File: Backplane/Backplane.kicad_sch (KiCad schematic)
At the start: 16 parts

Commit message: Backplane: Fix couple of errors
Fix messed up AR lines, add jumper to activate /AR15. Layout WIP (no power yet)
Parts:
- added JP1: Experimental, Connector_PinHeader_2.54mm:PinHeader_1x02_P2.54mm_Vertical, symbol Jumper:Jumper_2_Open
- added unit 2 of U_A5
- added unit 1 of U_B1
- added unit 2 of U_B5
- added unit 3 of U_B5
- J2: renamed from J?; footprint (none) -> Connector_IDC:IDC-Header_2x25_P2.54mm_Vertical
- R1, R2, R3, R4: renamed from R?; footprint (none) -> Resistor_THT:R_Axial_DIN0207_L6.3mm_D2.5mm_P10.16mm_Horizontal
- U_A1: footprint Package_DIP:DIP-28_W15.24mm -> Package_DIP:DIP-24_W10.16mm
- U_A2: footprint (none) -> DIP-16_W7.62mm
- U_A3, U_A4, U_A5, U_B1, U_B2, U_B3, U_B4, U_B5: footprint (none) -> Package_DIP:DIP-14_W7.62mm
- gave numbers to parts that had none: 1
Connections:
- net Gnd is gone; now on net GND: U_A2.7 (Gnd), U_A2.7 (Gnd)
- net Vcc is gone; now on net +5V: U_A2.14 (Vcc), U_A2.14 (Vcc)
- net GND: now also U_A5.10, U_A5.12, U_A5.13, U_A5.9, U_B1.1, U_B5.10, U_B5.4, U_B5.5, U_B5.9
- net Sys.~{RA_{11}}: no longer U_B2.13
- net Sys.~{RA_{13}}: now also J2.20 (Pin_20)
- net Sys.~{RA_{14}}: now also U_B2.13
- net Sys.~{RA_{15}}: now also JP1.2 (B)
- net at R1.2, R2.1, U_B3.5: now also JP1.1 (A)
- no-connect marks 13 -> 16
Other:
- moved on the sheet: R1, R2

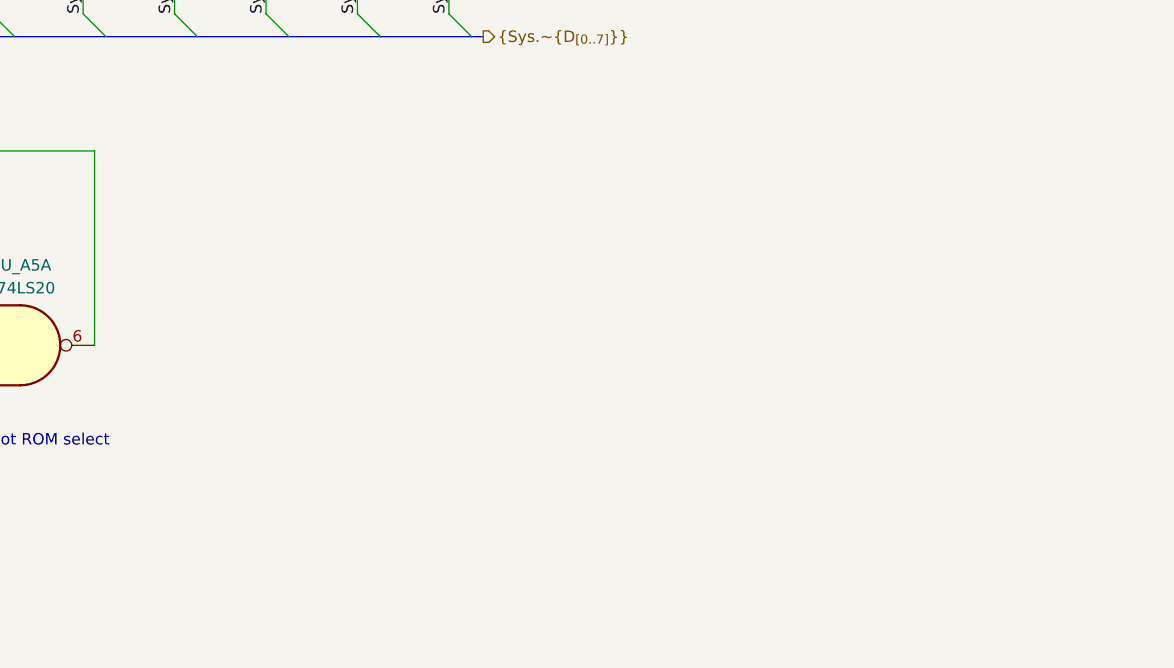
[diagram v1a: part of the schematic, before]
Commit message: Backplane: Completed
Full board layout
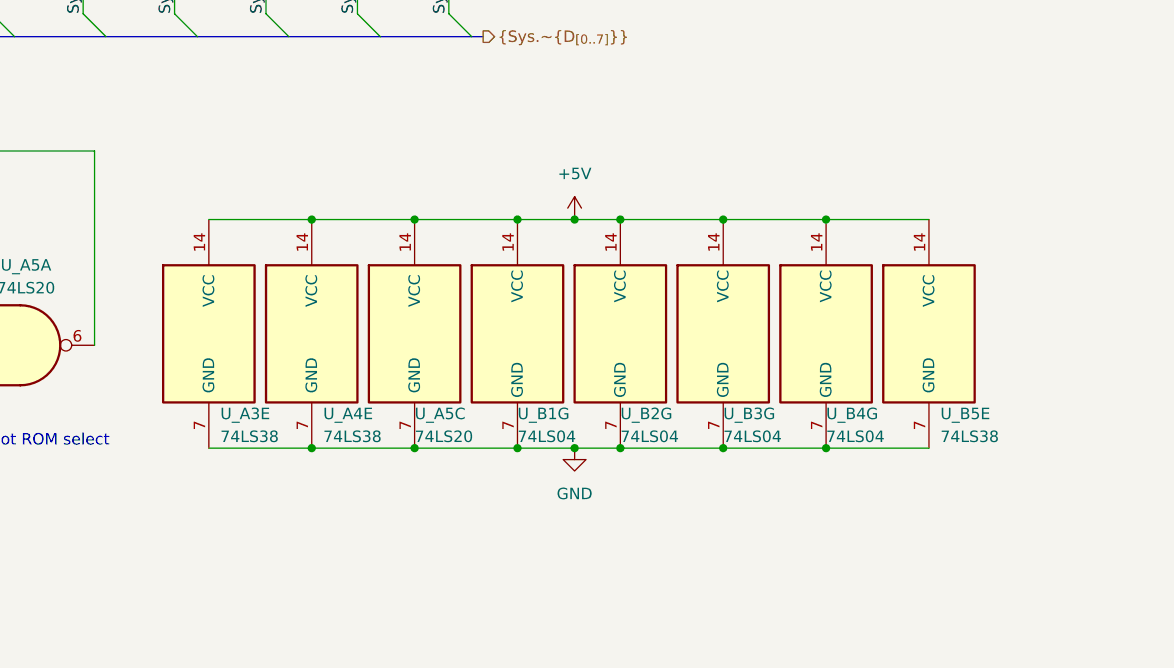
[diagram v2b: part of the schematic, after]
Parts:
- added unit 5 of U_A3
- added unit 5 of U_A4
- added unit 3 of U_A5
- added unit 7 of U_B1
- added unit 7 of U_B2
- added unit 7 of U_B3
- added unit 7 of U_B4
- added unit 5 of U_B5
- U_A2: footprint DIP-16_W7.62mm -> Package_DIP:DIP-14_W7.62mm
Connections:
- net +5V: now also U_A3.14 (VCC), U_A4.14 (VCC), U_A5.14 (VCC), U_B1.14 (VCC), U_B2.14 (VCC), U_B3.14 (VCC), U_B4.14 (VCC), U_B5.14 (VCC)
- net GND: now also U_A3.7 (GND), U_A4.7 (GND), U_A5.7 (GND), U_B1.7 (GND), U_B2.7 (GND), U_B3.7 (GND), U_B4.7 (GND), U_B5.7 (GND)

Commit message: Backplane: Polish up
Annotate connectors on silk screen, change ROM footprint to socketed one
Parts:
- U_A1: footprint Package_DIP:DIP-24_W10.16mm -> Package_DIP:DIP-24_W10.16mm_Socket
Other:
- title: (none) -> Centurion backplane, short
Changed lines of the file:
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@@
 (kicad_sch (version 20211123) (generator eeschema)
   (paper "A4")
+  (title_block
+    (title "Centurion backplane, short")
+    (rev "1.0")
+  )
   (junction (at 19.05 107.95) (diameter 0) (color 0 0 0 0)
   )
@@
   (symbol (lib_id "power:+5V") (at 236.22 125.73 0) (unit 1)
     (in_bom yes) (on_board yes) (fields_autoplaced)
-    (property "Reference" "#PWR?" (id 0) (at 236.22 129.54 0)
+    (property "Reference" "#PWR0123" (id 0) (at 236.22 129.54 0)
       (effects (font (size 1.27 1.27)) hide)
     )
@@
       (effects (font (size 1.27 1.27)) (justify left))
     )
-    (property "Footprint" "Package_DIP:DIP-24_W10.16mm" (id 2) (at 210.82 74.93 0)
+    (property "Footprint" "Package_DIP:DIP-24_W10.16mm_Socket" (id 2) (at 210.82 74.93 0)
       (effects (font (size 1.27 1.27)) hide)
     )
@@
       (reference "#PWR0122") (unit 1) (value "GND") (footprint "")
     )
+    (path "/bd3178ab-c3d1-48e2-8657-6f2f9c3f17fc"
+      (reference "#PWR0123") (unit 1) (value "+5V") (footprint "")
+    )
     (path "/92741a45-2c80-49a0-b822-dc307fb28e0e"
       (reference "#PWR0124") (unit 1) (value "GND") (footprint "")
     )
-    (path "/bd3178ab-c3d1-48e2-8657-6f2f9c3f17fc"
-      (reference "#PWR?") (unit 1) (value "+5V") (footprint "")
-    )
     (path "/2fae2e1f-a694-4160-a6f3-1a6beed67fe7"
       (reference "J1") (unit 1) (value "Front panel") (footprint "Connector_IDC:IDC-Header_2x25_P2.54mm_Vertical")
@@
     )
     (path "/d8a6c379-193f-4aef-93b8-a8eb5ed3d15a"
-      (reference "U_A1") (unit 1) (value "3604") (footprint "Package_DIP:DIP-24_W10.16mm")
+      (reference "U_A1") (unit 1) (value "3604") (footprint "Package_DIP:DIP-24_W10.16mm_Socket")
     )
     (path "/c4c90f89-c7ff-49fa-b875-d46a735819c8"

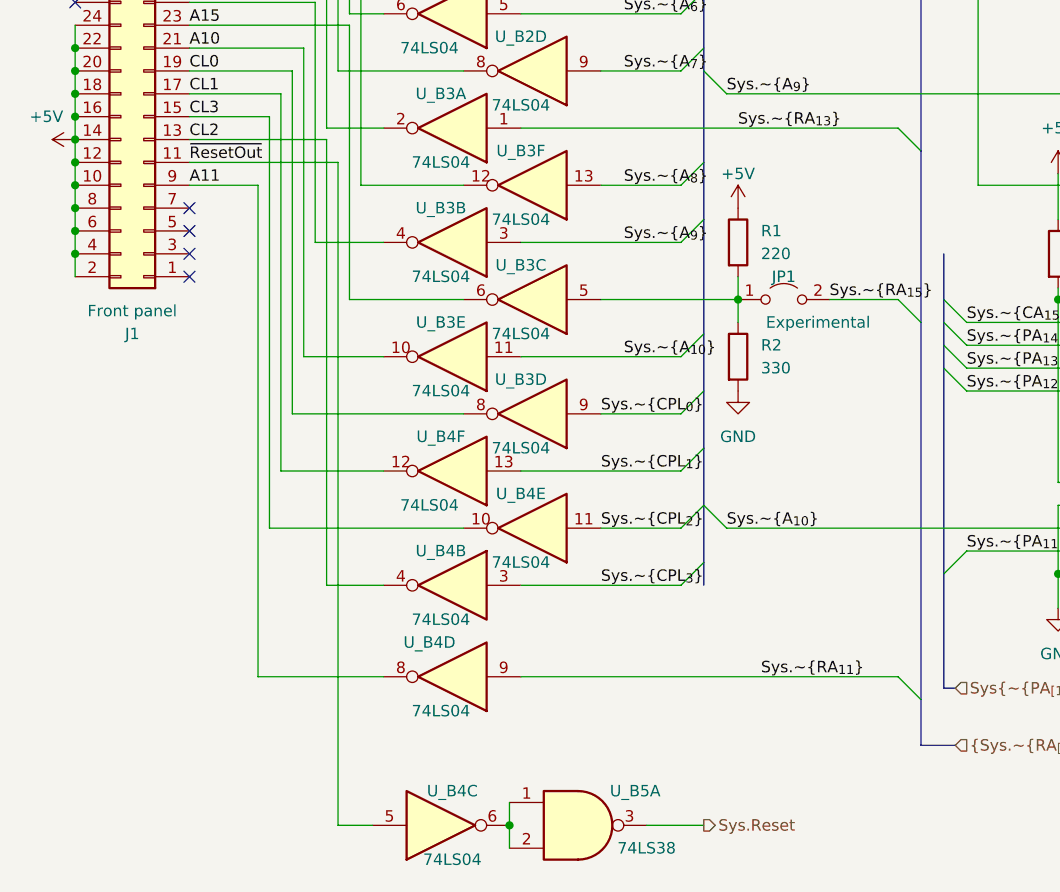
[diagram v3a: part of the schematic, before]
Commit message: Backplane: Fix RA15 signal
Original schematic by Nakazoto contained an error, which has been fixed. So no
need for an experimental jumper on RA15 line; and 220-330 divider actually sits
on a Reset signal, coming from the front panel.
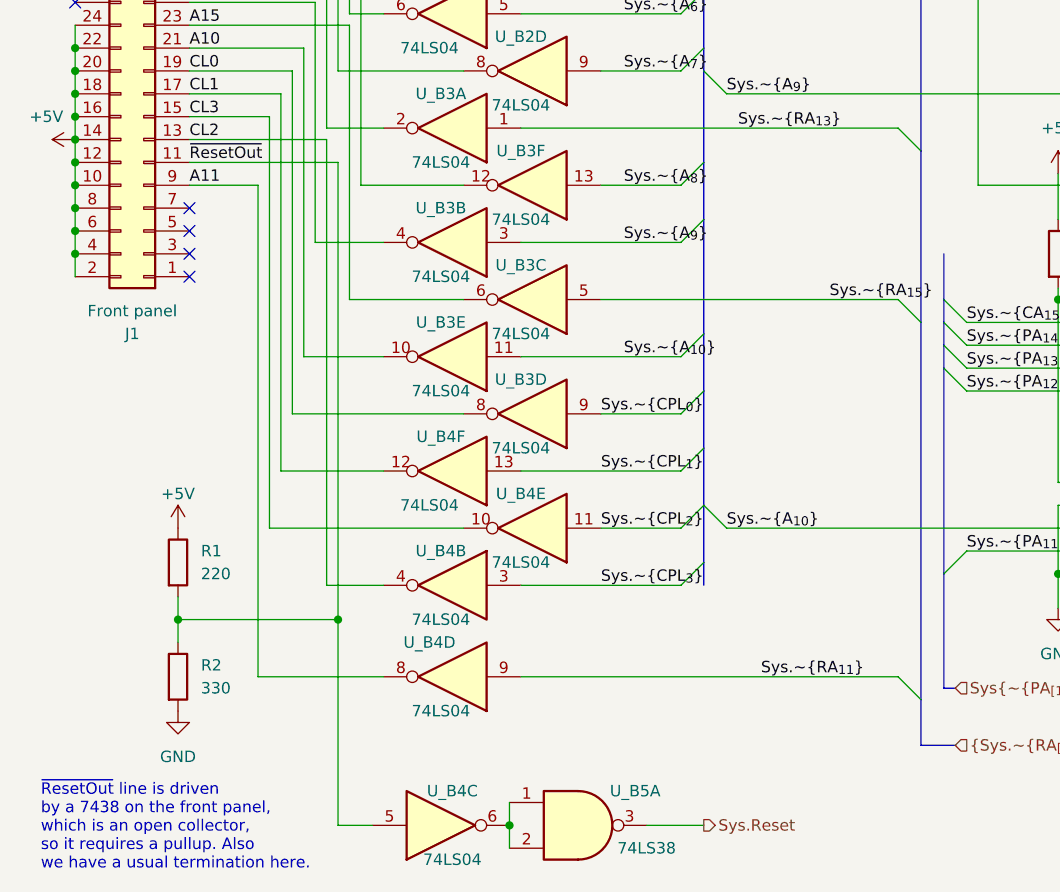
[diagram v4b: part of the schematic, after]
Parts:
- removed JP1: Experimental, Connector_PinHeader_2.54mm:PinHeader_1x02_P2.54mm_Vertical, symbol Jumper:Jumper_2_Open
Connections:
- net Sys.~{RA_{15}}: now also U_B3.5
- net ~{ResetOut}: now also R1.2, R2.1
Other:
- note added: "~{ResetOut} line is driven by a 7438 on the front panel, which is an open collector, so it requires a pullup. Also we have a usual termination here."

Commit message: Backplane: Modular design
Make sure that a horizontal bus connector can be installed, thus extending this
shortened backplane PCB to a full size, if PCB-mounted edge slots can be
purchased.
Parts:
- J2: footprint Connector_IDC:IDC-Header_2x25_P2.54mm_Vertical -> Connector_PinHeader_2.54mm:PinHeader_2x25_P2.54mm_Horizontal
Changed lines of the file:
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@@
     (property "Reference" "J2" (id 0) (at 256.54 21.59 0))
     (property "Value" "System bus" (id 1) (at 256.54 24.13 0))
-    (property "Footprint" "Connector_IDC:IDC-Header_2x25_P2.54mm_Vertical" (id 2) (at 255.27 58.42 0)
+    (property "Footprint" "Connector_PinHeader_2.54mm:PinHeader_2x25_P2.54mm_Horizontal" (id 2) (at 255.27 58.42 0)
       (effects (font (size 1.27 1.27)) hide)
     )
@@
     )
     (path "/3c650ba4-b8b7-493f-9028-99f0e30e52ce"
-      (reference "J2") (unit 1) (value "System bus") (footprint "Connector_IDC:IDC-Header_2x25_P2.54mm_Vertical")
+      (reference "J2") (unit 1) (value "System bus") (footprint "Connector_PinHeader_2.54mm:PinHeader_2x25_P2.54mm_Horizontal")
     )
     (path "/2da09754-df0a-400a-aca6-b8f5a82d0ae3"

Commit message: Backplane: Erratum E001
Incorrect U_A1 chip width
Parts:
- U_A1: footprint Package_DIP:DIP-24_W10.16mm_Socket -> Package_DIP:DIP-24_W15.24mm
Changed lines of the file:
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@@
   (title_block
     (title "Centurion backplane, short")
-    (rev "1.0")
+    (rev "2.0")
   )
   (junction (at 19.05 107.95) (diameter 0) (color 0 0 0 0)
@@
       (effects (font (size 1.27 1.27)) (justify left))
     )
-    (property "Footprint" "Package_DIP:DIP-24_W10.16mm_Socket" (id 2) (at 210.82 74.93 0)
+    (property "Footprint" "Package_DIP:DIP-24_W15.24mm" (id 2) (at 210.82 74.93 0)
       (effects (font (size 1.27 1.27)) hide)
     )
@@
     )
     (path "/d8a6c379-193f-4aef-93b8-a8eb5ed3d15a"
-      (reference "U_A1") (unit 1) (value "3604") (footprint "Package_DIP:DIP-24_W10.16mm_Socket")
+      (reference "U_A1") (unit 1) (value "3604") (footprint "Package_DIP:DIP-24_W15.24mm")
     )
     (path "/c4c90f89-c7ff-49fa-b875-d46a735819c8"

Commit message: Backplane: Use socket for U_A1
Just for compliance, let's change U_A1 footprint to socket
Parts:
- U_A1: footprint Package_DIP:DIP-24_W15.24mm -> Package_DIP:DIP-24_W15.24mm_Socket
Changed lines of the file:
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@@
       (effects (font (size 1.27 1.27)) (justify left))
     )
-    (property "Footprint" "Package_DIP:DIP-24_W15.24mm" (id 2) (at 210.82 74.93 0)
+    (property "Footprint" "Package_DIP:DIP-24_W15.24mm_Socket" (id 2) (at 210.82 74.93 0)
       (effects (font (size 1.27 1.27)) hide)
     )
@@
     )
     (path "/d8a6c379-193f-4aef-93b8-a8eb5ed3d15a"
-      (reference "U_A1") (unit 1) (value "3604") (footprint "Package_DIP:DIP-24_W15.24mm")
+      (reference "U_A1") (unit 1) (value "3604") (footprint "Package_DIP:DIP-24_W15.24mm_Socket")
     )
     (path "/c4c90f89-c7ff-49fa-b875-d46a735819c8"

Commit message: Backplane: Update footprint in the schematic
Update footprint association, synchronize with the PCB. Add one more replacement
entry to the README
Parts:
- U_A3, U_A4, U_A5, U_B1, U_B2, U_B3, U_B4, U_B5: footprint (none) -> Package_DIP:DIP-14_W7.62mm
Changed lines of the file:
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@@
       (effects (font (size 1.27 1.27)) (justify left))
     )
-    (property "Footprint" "" (id 2) (at 218.44 138.43 0)
+    (property "Footprint" "Package_DIP:DIP-14_W7.62mm" (id 2) (at 218.44 138.43 0)
       (effects (font (size 1.27 1.27)) hide)
     )
@@
       (effects (font (size 1.27 1.27)) (justify left))
     )
-    (property "Footprint" "" (id 2) (at 264.16 138.43 0)
+    (property "Footprint" "Package_DIP:DIP-14_W7.62mm" (id 2) (at 264.16 138.43 0)
       (effects (font (size 1.27 1.27)) hide)
     )
@@
       (effects (font (size 1.27 1.27)) (justify left))
     )
-    (property "Footprint" "" (id 2) (at 275.59 138.43 0)
+    (property "Footprint" "Package_DIP:DIP-14_W7.62mm" (id 2) (at 275.59 138.43 0)
       (effects (font (size 1.27 1.27)) hide)
     )
@@
     (property "Reference" "U_B5" (id 0) (at 35.56 36.83 0))
     (property "Value" "74LS38" (id 1) (at 35.56 39.37 0))
-    (property "Footprint" "" (id 2) (at 27.94 41.91 0)
+    (property "Footprint" "Package_DIP:DIP-14_W7.62mm" (id 2) (at 27.94 41.91 0)
       (effects (font (size 1.27 1.27)) hide)
     )
@@
       (effects (font (size 1.27 1.27)) (justify left))
     )
-    (property "Footprint" "" (id 2) (at 229.87 138.43 0)
+    (property "Footprint" "Package_DIP:DIP-14_W7.62mm" (id 2) (at 229.87 138.43 0)
       (effects (font (size 1.27 1.27)) hide)
     )
@@
       (effects (font (size 1.27 1.27)) (justify left))
     )
-    (property "Footprint" "" (id 2) (at 241.3 138.43 0)
+    (property "Footprint" "Package_DIP:DIP-14_W7.62mm" (id 2) (at 241.3 138.43 0)
       (effects (font (size 1.27 1.27)) hide)
     )
@@
       (effects (font (size 1.27 1.27)) (justify left))
     )
-    (property "Footprint" "" (id 2) (at 195.58 138.43 0)
+    (property "Footprint" "Package_DIP:DIP-14_W7.62mm" (id 2) (at 195.58 138.43 0)
       (effects (font (size 1.27 1.27)) hide)
     )
@@
       (effects (font (size 1.27 1.27)) (justify left))
     )
-    (property "Footprint" "" (id 2) (at 252.73 138.43 0)
+    (property "Footprint" "Package_DIP:DIP-14_W7.62mm" (id 2) (at 252.73 138.43 0)
       (effects (font (size 1.27 1.27)) hide)
     )
@@
       (effects (font (size 1.27 1.27)) (justify left))
     )
-    (property "Footprint" "" (id 2) (at 207.01 138.43 0)
+    (property "Footprint" "Package_DIP:DIP-14_W7.62mm" (id 2) (at 207.01 138.43 0)
       (effects (font (size 1.27 1.27)) hide)
     )
@@
     )
     (path "/6309c89a-c6ba-4602-bca2-8e479f8b92c3"
-      (reference "U_A3") (unit 5) (value "74LS38") (footprint "")
+      (reference "U_A3") (unit 5) (value "74LS38") (footprint "Package_DIP:DIP-14_W7.62mm")
     )
     (path "/e5fa9e11-948f-4ad8-b43d-b61fdaa8b7f2"
@@
     )
     (path "/ae6dc4a6-d7ec-4442-a64b-2aca8d4e9c59"
-      (reference "U_A4") (unit 5) (value "74LS38") (footprint "")
+      (reference "U_A4") (unit 5) (value "74LS38") (footprint "Package_DIP:DIP-14_W7.62mm")
     )
     (path "/75316ccb-fb98-4f82-bb56-50ebff116b4b"
@@
     )
     (path "/0490e272-c954-4c42-ad42-f98e6fdba02c"
-      (reference "U_A5") (unit 3) (value "74LS20") (footprint "")
+      (reference "U_A5") (unit 3) (value "74LS20") (footprint "Package_DIP:DIP-14_W7.62mm")
     )
     (path "/fbdd1d1c-a07c-4087-a34f-9c3a5a21399d"
@@
     )
     (path "/1ba543e9-937a-4e45-b282-36933a47713d"
-      (reference "U_B1") (unit 7) (value "74LS04") (footprint "")
+      (reference "U_B1") (unit 7) (value "74LS04") (footprint "Package_DIP:DIP-14_W7.62mm")
     )
     (path "/5b0a6592-1467-451a-b5fe-791564725bb2"
@@
     )
     (path "/208ed32a-087c-4898-a889-f51e7a5324c1"
-      (reference "U_B2") (unit 7) (value "74LS04") (footprint "")
+      (reference "U_B2") (unit 7) (value "74LS04") (footprint "Package_DIP:DIP-14_W7.62mm")
     )
     (path "/43a39be8-9e70-4a43-8649-b5aa7a301401"
@@
     )
     (path "/83855965-ad11-4099-a355-f928c2a766db"
-      (reference "U_B3") (unit 7) (value "74LS04") (footprint "")
+      (reference "U_B3") (unit 7) (value "74LS04") (footprint "Package_DIP:DIP-14_W7.62mm")
     )
     (path "/803747cb-ba89-45ea-8e6c-708115df2480"
@@
     )
     (path "/0a3116f4-a3c0-4992-8dd8-a4fef7bcad72"
-      (reference "U_B4") (unit 7) (value "74LS04") (footprint "")
+      (reference "U_B4") (unit 7) (value "74LS04") (footprint "Package_DIP:DIP-14_W7.62mm")
     )
     (path "/a72a490c-9c44-4a7c-978c-c6e2c5a242a3"
@@
     )
     (path "/12c59941-af50-4c39-8319-7d188e37846b"
-      (reference "U_B5") (unit 2) (value "74LS38") (footprint "")
+      (reference "U_B5") (unit 2) (value "74LS38") (footprint "Package_DIP:DIP-14_W7.62mm")
     )
     (path "/79ef2503-8cd4-45df-addd-94203ceb7a69"
@@
     )
     (path "/0b8f5189-1c1f-49aa-ae3c-4ac50debfffc"
-      (reference "U_B5") (unit 5) (value "74LS38") (footprint "")
-    )
-  )
+      (reference "U_B5") (unit 5) (value "74LS38") (footprint "Package_DIP:DIP-14_W7.62mm")
+    )
+  )
